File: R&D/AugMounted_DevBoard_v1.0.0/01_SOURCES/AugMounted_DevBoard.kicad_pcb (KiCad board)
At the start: 4 copper layers, 55.7 x 82.9 mm, 144 parts, among them J201 J_TYPE-C-31-M-13, J301 J_JST_S2B-PH-SM4-TB, J401 J_FH43BW-61S-0.2SHW, J501 J_0788641001_PAD, J502 J_0788641001, J503 J_0788641001, J504 J_0788641001_PAD, Q301 Q_BSS123WQ-7-F, Q302 Q_HSS2P10, Q303 Q_BSS123WQ-7-F, Q304 Q_HSS2P10, Q305 Q_BSS123WQ-7-F, Q306 Q_BSS123WQ-7-F, Q307 Q_HSS2P10, Q501 Q_BSS123WQ-7-F, SW501 SW_SKRTLAE010, SW601 SW_EC12D1564404, SW602 SW_SKRTLAE010, SW603 SW_SKRTLAE010, U201 ESP32-S3-WROOM-1U-N16R8, U202 U_MCP23017T-E/ML, U301 U_LP3987H-18B5F, U302 U_MAX17048G+T10, U303 U_BQ24296MRGER, U304 U_TPS63001DRCR, U305 U_TPS61087DRCR, U401 U_TXS0108E, U402 U_TXS0108E, U403 U_TXS0108E, U501 U_VCNL4040M3OE, U502 ICS‐41350, U503 LIS2DW12

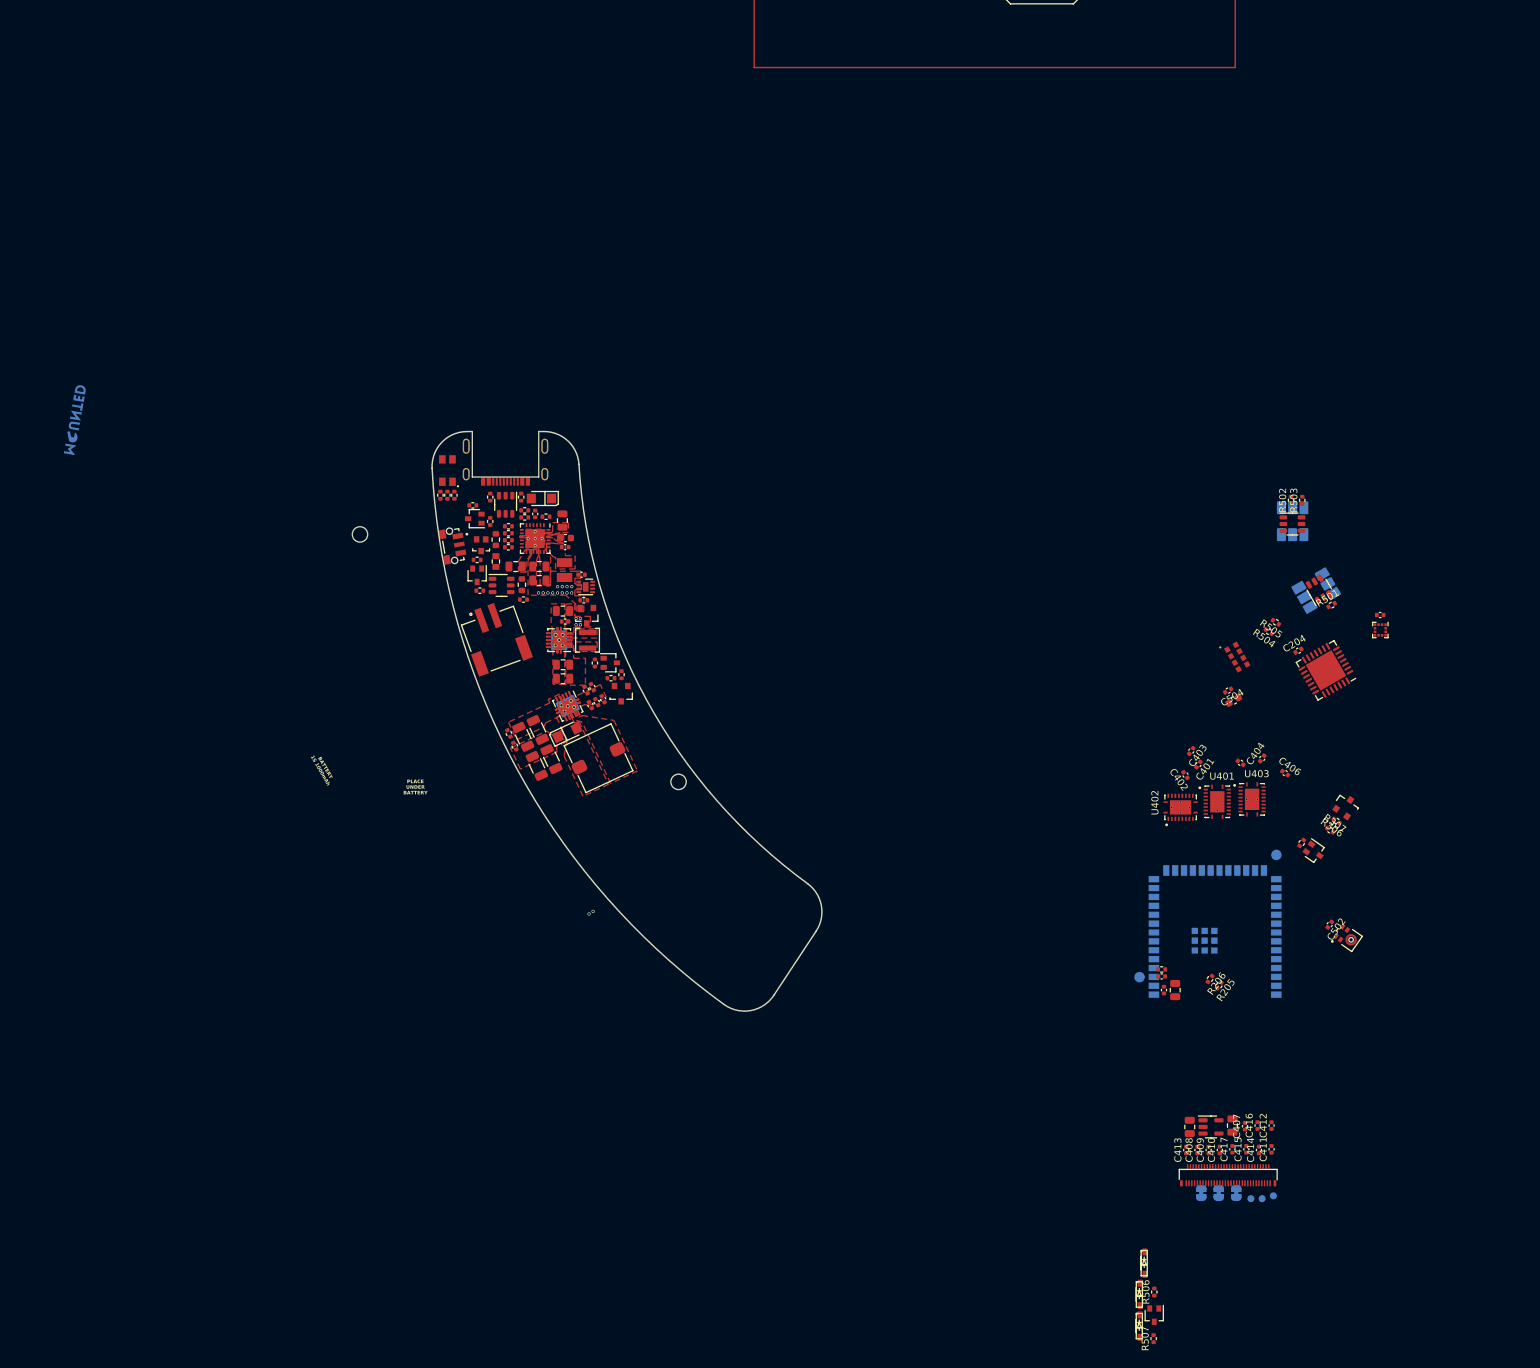
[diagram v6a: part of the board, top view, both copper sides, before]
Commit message: Component layout is done, routing video signals is done too.
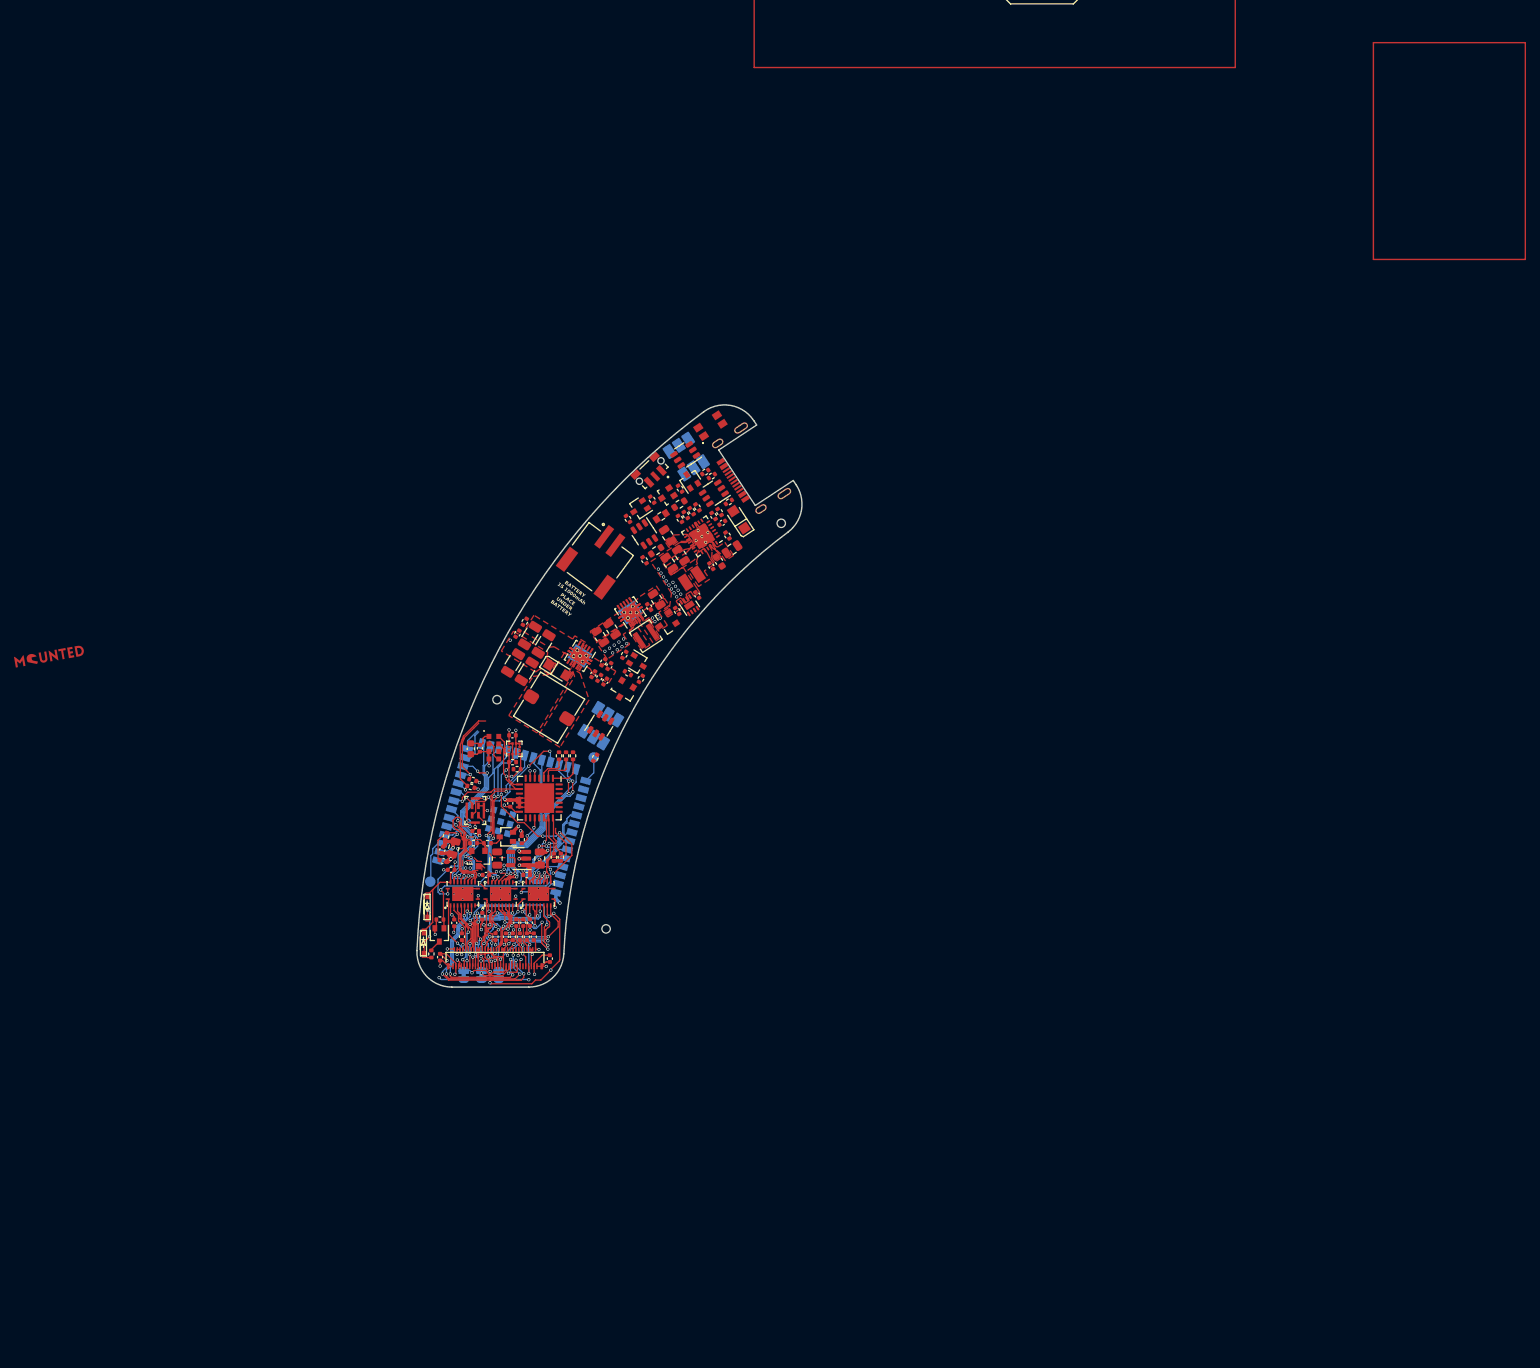
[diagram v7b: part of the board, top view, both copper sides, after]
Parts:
- removed H102: MountingHole, MountingHole:MountingHole_2.2mm_M2
- removed LED501: LED_LTW-010DCG, .mounted-lib:LED_LTW-010DCG
- removed TP401, TP402, TP403: TESTPOINT_1MM, .mounted-lib:TESTPOINT_1MM
- added H103: H_MOUNTING_HOLE_M1, .mounted-lib:MountingHole_1.2mm_M1, F.Cu at (197.1, 41.5)
- added H104: H_MOUNTING_HOLE_M1, .mounted-lib:MountingHole_1.2mm_M1, F.Cu at (172.0, 99.5)
- H101: value MountingHole -> H_MOUNTING_HOLE_M1; footprint MountingHole:MountingHole_2.2mm_M2 -> .mounted-lib:MountingHole_1.2mm_M1
- LOGO101: moved to F.Cu
- U502: value ICS‐41350 -> MP34DT05TR-A; footprint .mounted-lib:U_ICS-41350 -> .mounted-lib:U_MP34DT05TR-A
- moved U502 126.0 mm to (153.3, 82.5), turned to 180 degrees
- moved C503 125.3 mm to (158.7, 71.8), turned to 0 degrees
- moved R503 125.2 mm to (153.0, 78.2), turned to 165 degrees
- moved U503 125.0 mm to (158.9, 73.7), turned to 90 degrees
- moved Q302 124.3 mm to (153.8, 89.4), turned to -90 degrees
- moved R502 124.3 mm to (152.7, 79.2), turned to 165 degrees
- moved R306 123.5 mm to (153.1, 87.2), turned to 0 degrees
- moved C502 122.9 mm to (153.4, 85.5), turned to 180 degrees
- moved C406 120.7 mm to (150.3, 98.6), turned to -90 degrees
- moved R307 120.5 mm to (155.1, 87.2), turned to 0 degrees
- moved R507 117.0 mm to (147.1, 103.1)
- moved LED503 116.1 mm to (145.9, 101.5)
- moved LED502 115.9 mm to (146.5, 96.3)
- moved Q501 115.8 mm to (148.2, 100.3)
- moved Q301 115.6 mm to (157.8, 86.3), turned to 180 degrees
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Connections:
- D502 pad 4: /BUTTON2 -> /BUTTON1
- D502 pad 6: /BUTTON1 -> /BUTTON2
- J401 pad 46: Net-(J401-TEST(DDEN)) -> unconnected-(J401-TEST(DDEN)-Pad46)
- J401 pad 51: Net-(J401-TEST-Pad51) -> unconnected-(J401-TEST-Pad51)
- J401 pad 52: Net-(J401-TEST-Pad52) -> unconnected-(J401-TEST-Pad52)
- U201 pad 18: /B5 -> /G4
- U201 pad 19: /B4 -> /G5
- U201 pad 20: /B3 -> /G3
- U201 pad 21: /B2 -> /B1
- U201 pad 22: /B1 -> /B2
- U201 pad 24: /G5 -> /B4
- U201 pad 25: /G4 -> /B5
- U201 pad 26: /G3 -> /B3
- U502 pad 1: /I2S_PDM_DATA -> +3.3V
- U502 pad 3: GND -> /I2S_PDM_CLK
- U502 pad 4: /I2S_PDM_CLK -> /I2S_PDM_DATA
- U502 pad 5: +3.3V -> GND
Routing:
- net GND: track 1.48 -> 93.4 mm, vias 0 -> 36
- net +3.3V: track 0.00 -> 47.5 mm, vias 0 -> 24
- net /SCL: track 0.00 -> 34.8 mm, vias 0 -> 5
- net /MCLK: track 0.00 -> 33.1 mm, vias 0 -> 3
- net /LEDS_ENABLE: track 0.00 -> 32.3 mm, vias 0 -> 2
- net /OLED/MISO_1.8V: track 0.00 -> 27.2 mm, vias 0 -> 4
- net /OLED/MOSI_1.8V: track 0.00 -> 26.6 mm, vias 0 -> 4
- net /OLED/RGB_LSB_1.8V: track 0.00 -> 26.5 mm, vias 0 -> 2
- net /OLED/SCK_1.8V: track 0.00 -> 23.9 mm, vias 0 -> 4
- net /XCLR: track 0.00 -> 23.9 mm, vias 0 -> 3
- net /OLED/G3_1.8V: track 0.00 -> 23.9 mm, vias 0 -> 5
- net /G3: track 0.00 -> 23.3 mm, vias 0 -> 3
- net /SDA: track 0.00 -> 23.1 mm, vias 0 -> 3
- net /XHD: track 0.00 -> 23.1 mm, vias 0 -> 1
- net /B4: track 0.00 -> 23.0 mm, vias 0 -> 3
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- added copper zone on In2.Cu, net +10V
- added copper zone on F.Cu, net +1V8
- added copper zone on In2.Cu, net +1V8
- added copper zone on F.Cu, net /1.8V_LCD
- added copper zone on In2.Cu, net /1.8V_LCD
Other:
- board size 55.7 x 82.9 mm -> 55.1 x 83.3 mm

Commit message: Layout almost done
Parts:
- removed J502, J503: J_0788641001, .mounted-lib:J_788641001
- removed SW601: SW_EC12D1564404, .mounted-lib:SW_EC12D1564404
- removed SW602, SW603: SW_SKRTLAE010, .mounted-lib:SW_SKRTLAE010
- LOGO101: moved to B.Cu
- moved LOGO101 77.0 mm to (169.4, 63.3), turned to -10 degrees
- moved R202 9.88 mm to (167.9, 84.6), turned to 58.4 degrees
- moved R315 9.74 mm to (179.2, 56.4), turned to -56.6 degrees
- moved R203 9.37 mm to (167.1, 84.1), turned to -121.6 degrees
- moved R204 8.86 mm to (166.2, 83.5), turned to -121.6 degrees
- moved D502 8.57 mm to (172.4, 78.9)
- moved H101 8.46 mm to (157.8, 75.0)
- moved R205 8.28 mm to (160.2, 84.9)
- moved C413 8.26 mm to (149.0, 111.7)
- moved R310 8.26 mm to (175.4, 68.5)
- moved R505 8.26 mm to (166.3, 97.5)
- moved R318 8.26 mm to (175.9, 49.1)
- moved C405 8.26 mm to (155.1, 105.9)
- moved R313 8.26 mm to (183.4, 44.7)
- moved R306 8.26 mm to (153.8, 95.4)
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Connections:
- D201 pad 1: /MCU/USB_D+ -> /MCU/USB_D-
- D201 pad 3: /MCU/USB_D- -> /MCU/USB_D+
- D201 pad 4: /MCU/CC1 -> /MCU/CC2
- D201 pad 6: /MCU/CC2 -> /MCU/CC1
- U401 pad 10: /OLED/1.8V -> +1V8
- U402 pad 10: /OLED/1.8V -> +1V8
- U403 pad 10: /OLED/1.8V -> +1V8
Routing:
- net /Battery Management/ESP_POWER_EN: track 0.00 -> 86.8 mm, vias 0 -> 9
- net Net-(LED201-GA): track 0.00 -> 77.3 mm, vias 0 -> 6
- net /Battery Management/ENCODER_BUTTON: track 0.00 -> 69.4 mm, vias 0 -> 6
- net /Battery Management/PGOOD: track 0.00 -> 67.3 mm, vias 0 -> 6
- net /SCL: track 34.8 -> 101.3 mm, vias 5 -> 13
- net Net-(LED201-BA): track 0.00 -> 66.2 mm, vias 0 -> 2
- net /Battery Management/CHARGE_STATUS: track 0.00 -> 65.6 mm, vias 0 -> 6
- net Net-(LED201-RA): track 0.00 -> 63.1 mm, vias 0 -> 2
- net /MCU/USB_D+: track 3.22 -> 63.4 mm, vias 0 -> 3
- net /SDA: track 23.1 -> 82.6 mm, vias 3 -> 7
- net /ENCODER_B: track 13.8 -> 73.1 mm, vias 1 -> 6
- net /MCU/USB_D-: track 4.96 -> 64.2 mm, vias 0 -> 3
- net /ENCODER_A: track 10.9 -> 69.0 mm, vias 1 -> 5
- net /Battery Management/10V_ENABLE: track 0.00 -> 47.3 mm, vias 0 -> 4
- net /ENCODER_S1: track 0.00 -> 38.6 mm, vias 0 -> 2
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- added copper zone on F.Cu, net /Battery Management/VBAT_NOT_FUSED
- added copper zone on B.Cu, net GND
- added copper zone on F.Cu, net VBUS
- removed copper zone on In2.Cu, net VBUS
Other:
- board text added: "BATTERY Li-Ion 1S"
- board text removed: "BATTERY 1S 1000mAh"
- board text removed: "PLACE UNDER BATTERY"
